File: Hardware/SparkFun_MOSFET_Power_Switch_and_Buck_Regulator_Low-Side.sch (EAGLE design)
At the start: 42 parts, among them J1 PTH, J3 5.5x2.1mm Barrel, J4 SMD, Q1 600mA/40V, Q2 100A/100V/6.8mΩ, U1 LMR14203

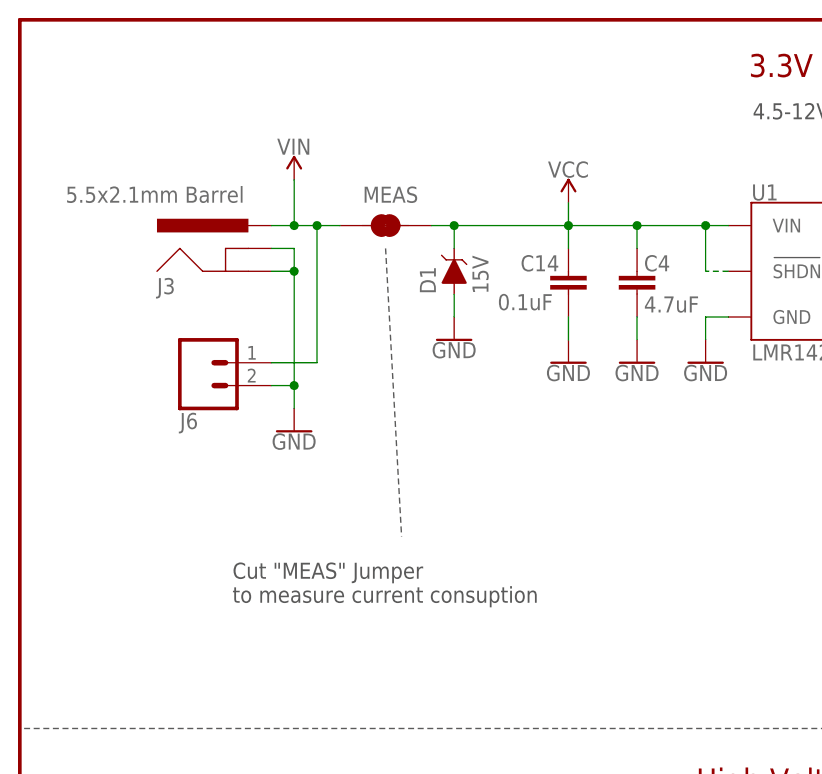
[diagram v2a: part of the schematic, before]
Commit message: Removed D1 Zener
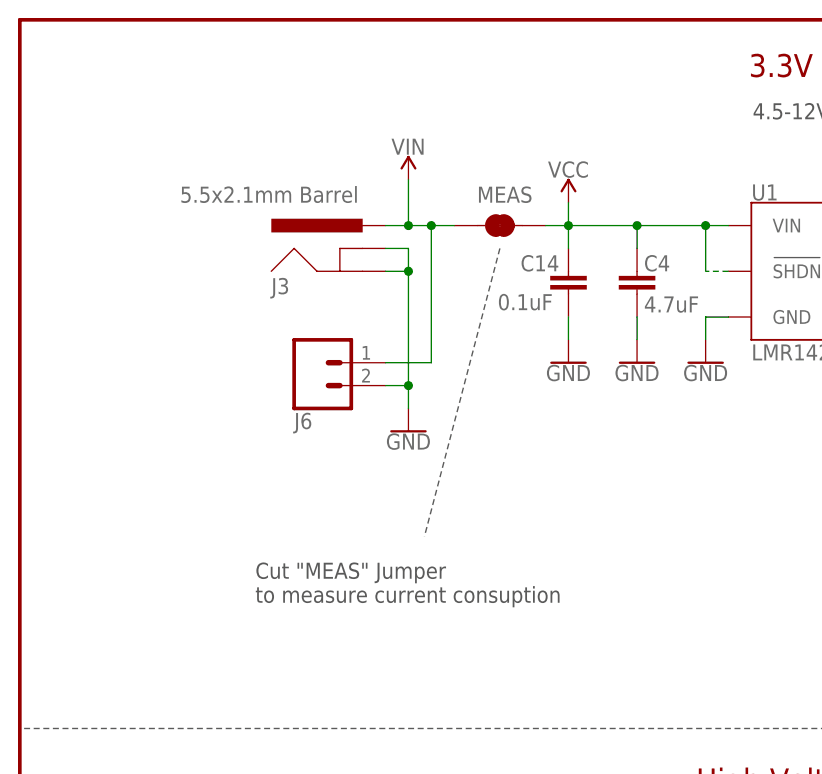
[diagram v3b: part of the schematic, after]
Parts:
- removed D1: 15V, SparkFun-DiscreteSemi:DIODE-ZENER-DZ2J150M0L
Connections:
- net GND: no longer D1.A
- net VCC: no longer D1.C
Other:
- moved on the sheet: J3, J6, MEAS
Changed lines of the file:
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@@
 <part name="R10" library="SparkFun-Resistors" deviceset="10KOHM" device="-0603-1/10W-1%" value="10k"/>
 <part name="D2" library="SparkFun-DiscreteSemi" deviceset="DIODE-SCHOTTKY" device="-MSS1P6-M3/89A" value="1A/60V/520mV"/>
-<part name="GND11" library="SparkFun-PowerSymbols" deviceset="GND" device=""/>
 <part name="J3" library="SparkFun-Connectors" deviceset="POWER_JACK" device="SMD" value="5.5x2.1mm Barrel"/>
 <part name="J5" library="SparkFun-Connectors" deviceset="CONN_02" device="SMALL_POKEHOME"/>
@@
 <part name="LOGO3" library="SparkFun-Aesthetics" deviceset="SPECIAL_INSTRUCTIONS" device="-ORDERING"/>
 <part name="SUPPLY1" library="SparkFun-PowerSymbols" deviceset="3.3V" device=""/>
-<part name="D1" library="SparkFun-DiscreteSemi" deviceset="DIODE-ZENER" device="-DZ2J150M0L" value="15V"/>
 </parts>
 <sheets>
@@
 <wire x1="158.242" y1="133.858" x2="140.97" y2="119.888" width="0.1524" layer="97" style="shortdash"/>
 <text x="232.156" y="131.572" size="1.778" layer="97" font="vector" rot="R180">(DNP)</text>
-<text x="23.622" y="120.65" size="1.778" layer="97" font="vector">Cut "MEAS" Jumper
+<text x="26.162" y="120.65" size="1.778" layer="97" font="vector">Cut "MEAS" Jumper
 to measure current consuption</text>
-<wire x1="40.64" y1="160.02" x2="42.418" y2="128.016" width="0.1524" layer="97" style="shortdash"/>
+<wire x1="53.34" y1="160.02" x2="44.958" y2="128.016" width="0.1524" layer="97" style="shortdash"/>
 </plain>
 <instances>
@@
 <attribute name="VALUE" x="86.614" y="61.976" size="1.016" layer="96" font="vector" rot="R90" align="top-left"/>
 </instance>
-<instance part="GND11" gate="1" x="48.26" y="149.86" smashed="yes">
-<attribute name="VALUE" x="48.26" y="149.606" size="1.778" layer="96" font="vector" align="top-center"/>
-</instance>
-<instance part="J3" gate="G$1" x="25.4" y="154.94" smashed="yes">
-<attribute name="VALUE" x="5.08" y="165.1" size="1.778" layer="96" font="vector"/>
-<attribute name="NAME" x="15.24" y="154.94" size="1.778" layer="95" font="vector"/>
+<instance part="J3" gate="G$1" x="38.1" y="154.94" smashed="yes">
+<attribute name="VALUE" x="17.78" y="165.1" size="1.778" layer="96" font="vector"/>
+<attribute name="NAME" x="27.94" y="154.94" size="1.778" layer="95" font="vector"/>
 </instance>
 <instance part="J5" gate="J1" x="218.44" y="73.66" smashed="yes" rot="R180">
@@
 <attribute name="NAME" x="220.98" y="68.072" size="1.778" layer="95" font="vector" rot="R180"/>
 </instance>
-<instance part="SUPPLY3" gate="G$1" x="30.48" y="167.64" smashed="yes">
-<attribute name="VALUE" x="30.48" y="170.434" size="1.778" layer="96" font="vector" align="bottom-center"/>
+<instance part="SUPPLY3" gate="G$1" x="43.18" y="167.64" smashed="yes">
+<attribute name="VALUE" x="43.18" y="170.434" size="1.778" layer="96" font="vector" align="bottom-center"/>
 </instance>
 <instance part="SUPPLY4" gate="G$1" x="60.96" y="165.1" smashed="yes">
@@
 <attribute name="VALUE" x="205.74" y="56.134" size="1.778" layer="96" font="vector" align="bottom-center"/>
 </instance>
-<instance part="MEAS" gate="JP1" x="40.64" y="162.56" smashed="yes">
-<attribute name="NAME" x="38.1" y="165.1" size="1.778" layer="95" font="vector"/>
+<instance part="MEAS" gate="JP1" x="53.34" y="162.56" smashed="yes">
+<attribute name="NAME" x="50.8" y="165.1" size="1.778" layer="95" font="vector"/>
 </instance>
 <instance part="SUPPLY8" gate="G$1" x="160.02" y="165.1" smashed="yes">
@@
 <instance part="FD3" gate="G$1" x="231.14" y="27.94" smashed="yes"/>
 <instance part="FD4" gate="G$1" x="233.68" y="27.94" smashed="yes"/>
-<instance part="J6" gate="J1" x="20.32" y="147.32" smashed="yes" rot="MR180">
-<attribute name="VALUE" x="17.78" y="152.146" size="1.778" layer="96" font="vector" rot="MR180"/>
-<attribute name="NAME" x="17.78" y="141.732" size="1.778" layer="95" font="vector" rot="MR180"/>
-</instance>
-<instance part="GND3" gate="1" x="30.48" y="139.7" smashed="yes">
-<attribute name="VALUE" x="30.48" y="139.446" size="1.778" layer="96" font="vector" align="top-center"/>
+<instance part="J6" gate="J1" x="33.02" y="147.32" smashed="yes" rot="MR180">
+<attribute name="VALUE" x="30.48" y="152.146" size="1.778" layer="96" font="vector" rot="MR180"/>
+<attribute name="NAME" x="30.48" y="141.732" size="1.778" layer="95" font="vector" rot="MR180"/>
+</instance>
+<instance part="GND3" gate="1" x="43.18" y="139.7" smashed="yes">
+<attribute name="VALUE" x="43.18" y="139.446" size="1.778" layer="96" font="vector" align="top-center"/>
 </instance>
 <instance part="LOGO3" gate="G$1" x="226.06" y="33.02" smashed="yes"/>
 <instance part="SUPPLY1" gate="G$1" x="53.34" y="76.2" smashed="yes">
 <attribute name="VALUE" x="53.34" y="78.994" size="1.778" layer="96" font="vector" align="bottom-center"/>
-</instance>
-<instance part="D1" gate="G$1" x="48.26" y="157.48" smashed="yes" rot="R90">
-<attribute name="NAME" x="46.228" y="154.94" size="1.778" layer="95" font="vector" rot="R90"/>
-<attribute name="VALUE" x="50.292" y="154.94" size="1.778" layer="96" font="vector" rot="R90" align="top-left"/>
 </instance>
 </instances>
@@
 </segment>
 <segment>
-<wire x1="27.94" y1="157.48" x2="30.48" y2="157.48" width="0.1524" layer="91"/>
-<wire x1="27.94" y1="160.02" x2="30.48" y2="160.02" width="0.1524" layer="91"/>
+<wire x1="40.64" y1="157.48" x2="43.18" y2="157.48" width="0.1524" layer="91"/>
+<wire x1="40.64" y1="160.02" x2="43.18" y2="160.02" width="0.1524" layer="91"/>
 <pinref part="J3" gate="G$1" pin="GNDBREAK"/>
 <pinref part="J3" gate="G$1" pin="GND"/>
-<wire x1="30.48" y1="157.48" x2="30.48" y2="144.78" width="0.1524" layer="91"/>
-<junction x="30.48" y="157.48"/>
+<wire x1="43.18" y1="157.48" x2="43.18" y2="144.78" width="0.1524" layer="91"/>
+<junction x="43.18" y="157.48"/>
 <pinref part="J6" gate="J1" pin="2"/>
-<wire x1="27.94" y1="144.78" x2="30.48" y2="144.78" width="0.1524" layer="91"/>
+<wire x1="40.64" y1="144.78" x2="43.18" y2="144.78" width="0.1524" layer="91"/>
 <pinref part="GND3" gate="1" pin="GND"/>
-<wire x1="30.48" y1="144.78" x2="30.48" y2="142.24" width="0.1524" layer="91"/>
-<junction x="30.48" y="144.78"/>
-<wire x1="30.48" y1="160.02" x2="30.48" y2="157.48" width="0.1524" layer="91"/>
+<wire x1="43.18" y1="144.78" x2="43.18" y2="142.24" width="0.1524" layer="91"/>
+<junction x="43.18" y="144.78"/>
+<wire x1="43.18" y1="160.02" x2="43.18" y2="157.48" width="0.1524" layer="91"/>
 </segment>
 <segment>
@@
 <wire x1="160.02" y1="129.54" x2="160.02" y2="127" width="0.1524" layer="91"/>
 <pinref part="PWR_LED" gate="G$1" pin="1"/>
-</segment>
-<segment>
-<pinref part="D1" gate="G$1" pin="A"/>
-<pinref part="GND11" gate="1" pin="GND"/>
-<wire x1="48.26" y1="152.4" x2="48.26" y2="154.94" width="0.1524" layer="91"/>
 </segment>
 </net>
@@
 <net name="VIN" class="0">
 <segment>
-<wire x1="27.94" y1="162.56" x2="30.48" y2="162.56" width="0.1524" layer="91"/>
+<wire x1="40.64" y1="162.56" x2="43.18" y2="162.56" width="0.1524" layer="91"/>
 <pinref part="J3" gate="G$1" pin="PWR"/>
 <pinref part="SUPPLY3" gate="G$1" pin="VIN"/>
 <pinref part="MEAS" gate="JP1" pin="1"/>
-<wire x1="30.48" y1="162.56" x2="33.02" y2="162.56" width="0.1524" layer="91"/>
-<wire x1="33.02" y1="162.56" x2="35.56" y2="162.56" width="0.1524" layer="91"/>
-<wire x1="33.02" y1="162.56" x2="33.02" y2="147.32" width="0.1524" layer="91"/>
-<junction x="33.02" y="162.56"/>
+<wire x1="43.18" y1="162.56" x2="45.72" y2="162.56" width="0.1524" layer="91"/>
+<wire x1="45.72" y1="162.56" x2="48.26" y2="162.56" width="0.1524" layer="91"/>
+<wire x1="45.72" y1="162.56" x2="45.72" y2="147.32" width="0.1524" layer="91"/>
+<junction x="45.72" y="162.56"/>
 <pinref part="J6" gate="J1" pin="1"/>
-<wire x1="33.02" y1="147.32" x2="27.94" y2="147.32" width="0.1524" layer="91"/>
-<wire x1="30.48" y1="162.56" x2="30.48" y2="167.64" width="0.1524" layer="91"/>
-<junction x="30.48" y="162.56"/>
+<wire x1="45.72" y1="147.32" x2="40.64" y2="147.32" width="0.1524" layer="91"/>
+<wire x1="43.18" y1="162.56" x2="43.18" y2="167.64" width="0.1524" layer="91"/>
+<junction x="43.18" y="162.56"/>
 </segment>
 </net>
@@
 <pinref part="U1" gate="U1" pin="SHDN"/>
 <pinref part="U1" gate="U1" pin="VIN"/>
-<wire x1="45.72" y1="162.56" x2="48.26" y2="162.56" width="0.1524" layer="91"/>
 <junction x="60.96" y="162.56"/>
-<wire x1="48.26" y1="162.56" x2="60.96" y2="162.56" width="0.1524" layer="91"/>
+<wire x1="58.42" y1="162.56" x2="60.96" y2="162.56" width="0.1524" layer="91"/>
 <wire x1="60.96" y1="165.1" x2="60.96" y2="162.56" width="0.1524" layer="91"/>
 <pinref part="SUPPLY4" gate="G$1" pin="VCC"/>
 <pinref part="MEAS" gate="JP1" pin="2"/>
-<pinref part="D1" gate="G$1" pin="C"/>
-<wire x1="48.26" y1="160.02" x2="48.26" y2="162.56" width="0.1524" layer="91"/>
-<junction x="48.26" y="162.56"/>
-</segment>
-<segment>
+</segment>
+<segment>
